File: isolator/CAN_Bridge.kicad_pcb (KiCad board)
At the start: 2 copper layers, 45 parts, among them J1 BOOT1, J2 BOOT0, J3 Power in, J4 JTAG5, J5 USART1, J7 HIGHVOLTAGE CAN, J8 LOWVOLTAGE CAN, SW2 SW_Push, U1 STM32F105RBTx, U2 ISO1050DUB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

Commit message: update isolator PCB
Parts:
- moved H1 9.60 mm to (135.4, 61.4)
- moved C1 1.10 mm to (144.7, 102.2)
- moved H1 0.71 mm to (135.4, 110.0)
- moved U2 0.70 mm to (169.5, 101.7)
- moved R6 0.20 mm to (160.2, 65.6)
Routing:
- net GND: track 29.8 -> 30.9 mm, vias 24 -> 23
- net HV_CANH: track 13.2 -> 14.2 mm
- net HV_CANL: track 13.0 -> 14.0 mm
- net +3.3V: track 127.8 -> 128.5 mm
- net HV_TXD: track 15.3 -> 14.6 mm
- net HV_RXD: track 14.4 -> 13.7 mm
- net +5P: track 19.5 -> 20.2 mm
- net GND2: track 3.71 -> 4.41 mm
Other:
- board outline added: 64 x 57.6 mm
- board text added: "12.7mm"

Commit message: Tweaks to schematic
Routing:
- net GND: track 30.9 -> 35.4 mm
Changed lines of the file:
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@@
   (segment (start 157.6625 84.8375) (end 159.3 84.8375) (width 1) (layer "F.Cu") (net 1))
   (segment (start 139.9 85.1625) (end 139.5 85.5625) (width 0.5) (layer "F.Cu") (net 2))
+  (segment (start 177.275 79.115) (end 177.275 77.425) (width 1) (layer "F.Cu") (net 2))
   (segment (start 144.13 82.05) (end 144.13 83.43) (width 0.5) (layer "F.Cu") (net 2))
   (segment (start 144.13 83.43) (end 144.8 84.1) (width 0.5) (layer "F.Cu") (net 2))
+  (segment (start 162.61 105.51) (end 162.5 105.4) (width 1) (layer "F.Cu") (net 2))
   (segment (start 139.9 83.8) (end 139.9 85.1625) (width 0.5) (layer "F.Cu") (net 2))
   (segment (start 171.75 66.425) (end 171.675 66.425) (width 0.5) (layer "F.Cu") (net 2))
@@
   (segment (start 144.15 87.08) (end 144.15 85.5875) (width 0.3) (layer "F.Cu") (net 2))
   (segment (start 171.75 66.425) (end 171.75 66.45) (width 0.5) (layer "F.Cu") (net 2))
+  (segment (start 177.275 77.425) (end 177.5 77.2) (width 1) (layer "F.Cu") (net 2))
+  (segment (start 164.975 105.51) (end 162.61 105.51) (width 1) (layer "F.Cu") (net 2))
   (via (at 144.8 84.1) (size 0.8) (drill 0.4) (layers "F.Cu" "B.Cu") (free) (net 2))
   (via (at 132.1 97.8) (size 0.8) (drill 0.4) (layers "F.Cu" "B.Cu") (free) (net 2))
@@
       (pts
         (xy 175.8 96.9)
-        (xy 172.6 96.9)
-        (xy 172.6 106.6)
+        (xy 175.8 96.9)
+        (xy 175.8 106.6)
         (xy 175.8 106.6)
         (xy 175.8 114.5)
@@
     (polygon
       (pts
-        (xy 166.4 106.5)
+        (xy 162.8 106.5)
         (xy 162.8 106.5)
         (xy 162.8 114.5)
@@
         (xy 130.9 56.9)
         (xy 194.9 56.9)
-        (xy 194.812446 77.4)
-        (xy 194.3 77.4)
-        (xy 194.3 80.2)
-        (xy 175.8 80.2)
+        (xy 194.812446 77.5)
+        (xy 194.3 77.5)
+        (xy 194.3 77.5)
+        (xy 175.8 77.5)
         (xy 175.8 77.5)
         (xy 170 77.5)
         (xy 162.8 85.9)
         (xy 162.8 96.8)
-        (xy 166.4 96.8)
+        (xy 162.8 96.8)
       )
     )

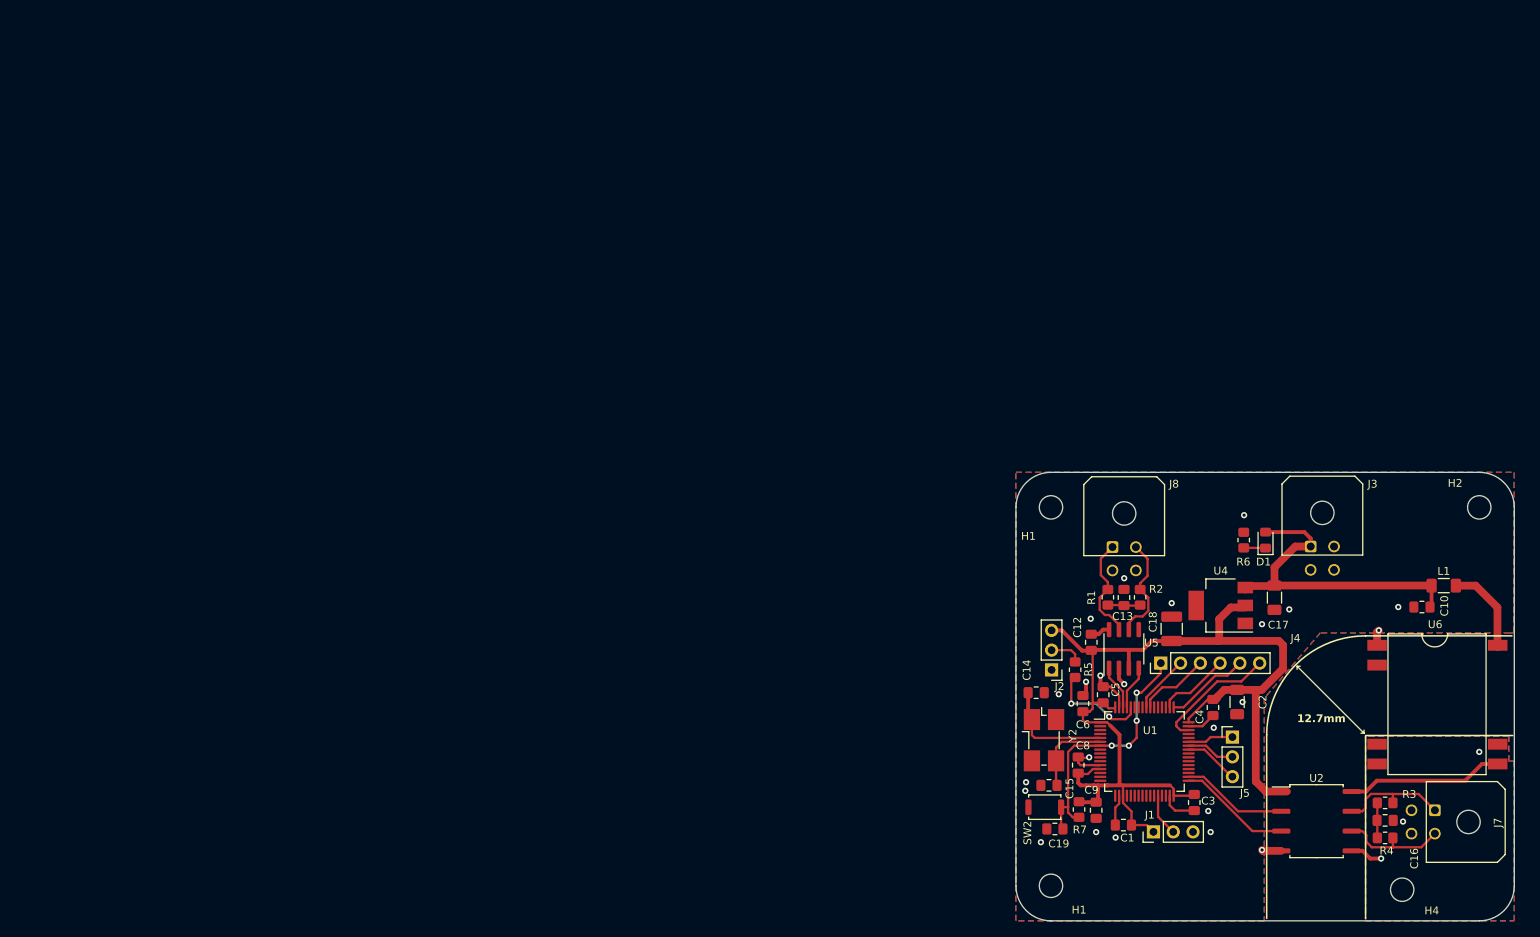
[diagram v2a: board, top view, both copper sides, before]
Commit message: Isolator tweaks
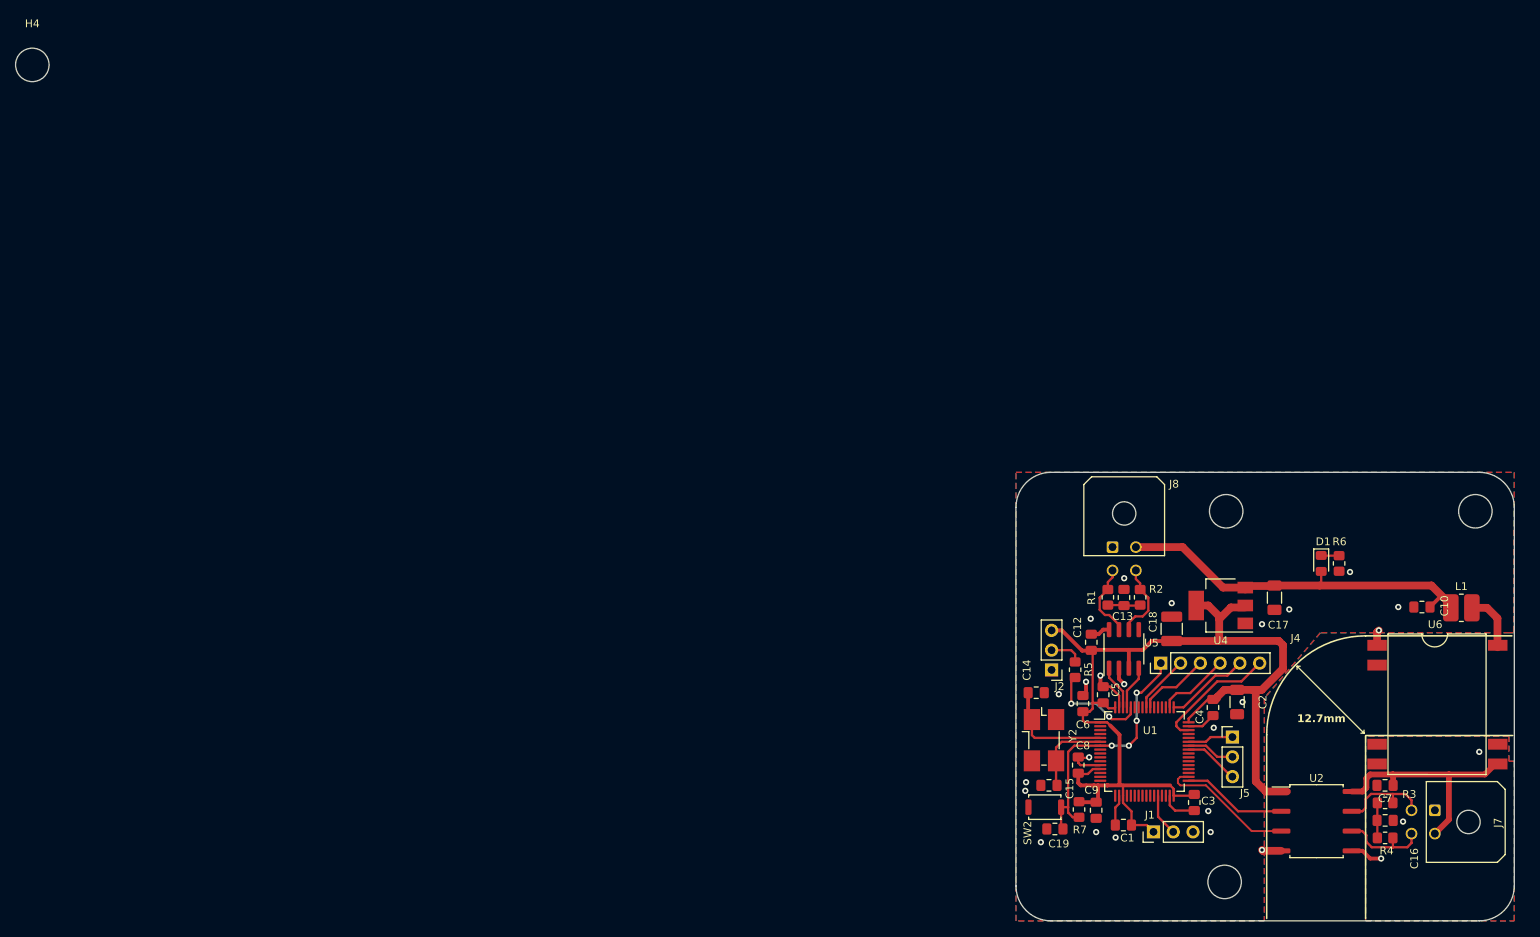
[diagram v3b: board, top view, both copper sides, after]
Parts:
- removed the H1 at (135.4, 110.0)
- removed the H1 at (135.4, 61.4)
- removed J3: Power in, Connector_Molex:Molex_Micro-Fit_3.0_43045-0400_2x02_P3.00mm_Horizontal
- added C7: 10u, Capacitor_SMD:C_0805_2012Metric_Pad1.18x1.45mm_HandSolder, F.Cu at (178.3, 97.1)
- added H1: MountingHole, MountingHole:MountingHole_4.3mm_M4, F.Cu at (157.7, 109.5)
- added H3: MountingHole, MountingHole:MountingHole_4.3mm_M4, F.Cu at (189.9, 61.9)
- H2, H4: footprint MountingHole:MountingHole_3mm -> MountingHole:MountingHole_4.3mm_M4
- L1: footprint Capacitor_SMD:C_1206_3216Metric_Pad1.33x1.80mm_HandSolder -> SUFST:RLS-397
- U4: footprint Package_TO_SOT_SMD:SOT-223 -> Package_TO_SOT_SMD:SOT-223-3_TabPin2
- U6: footprint Library:SMDIP-14_15.5mm -> SUFST:SMDIP-14_15.5mm
- Y2: value Crystal_GND24_Small -> 406C35E25M00000
- moved H4 205.4 mm to (4.58, 4.58)
- moved H2 32.5 mm to (157.9, 61.9)
- moved R6 12.6 mm to (172.4, 68.6), turned to 90 degrees
- moved D1 7.75 mm to (170.1, 68.6), turned to -90 degrees
- moved L1 3.64 mm to (188.1, 74.3)
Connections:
- net LV_RXD renamed MCU_CAN1_TX
- net LV_TXD renamed MCU_CAN1_RX
- J7 pad 1: HV_CANH -> GND2
- J7 pad 2: HV_CANL -> +5P
- J7 pad 3: (no net) -> HV_CANH
- J7 pad 4: (no net) -> HV_CANL
- J8 pad 1: LV_CANH -> GND
- J8 pad 2: LV_CANL -> +12V
- J8 pad 3: (no net) -> LV_CANH
- J8 pad 4: (no net) -> LV_CANL
- U1 pad 33: HV_TXD -> MCU_CAN2_RX
- U1 pad 34: HV_RXD -> MCU_CAN2_TX
- U2 pad 2: HV_RXD -> MCU_CAN2_RX
- U2 pad 3: HV_TXD -> MCU_CAN2_TX
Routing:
- net MCU_CAN2_TX: track 0.00 -> 17.8 mm
- net HV_TXD: track 14.6 -> 0.00 mm
- net HV_RXD: track 13.7 -> 0.00 mm
- net MCU_CAN2_RX: track 0.00 -> 13.5 mm
- net +5P: track 20.2 -> 30.7 mm
- net +12V: track 42.2 -> 50.2 mm
- net Net-(U6-+VIN): track 11.2 -> 7.17 mm
- net +3.3V: track 128.5 -> 132.4 mm
- net LV_CANL: track 14.2 -> 10.4 mm
- net LV_CANH: track 13.4 -> 9.63 mm
- net HV_CANL: track 14.0 -> 11.7 mm
- net HV_CANH: track 14.2 -> 12.0 mm

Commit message: Isolator done, pending review
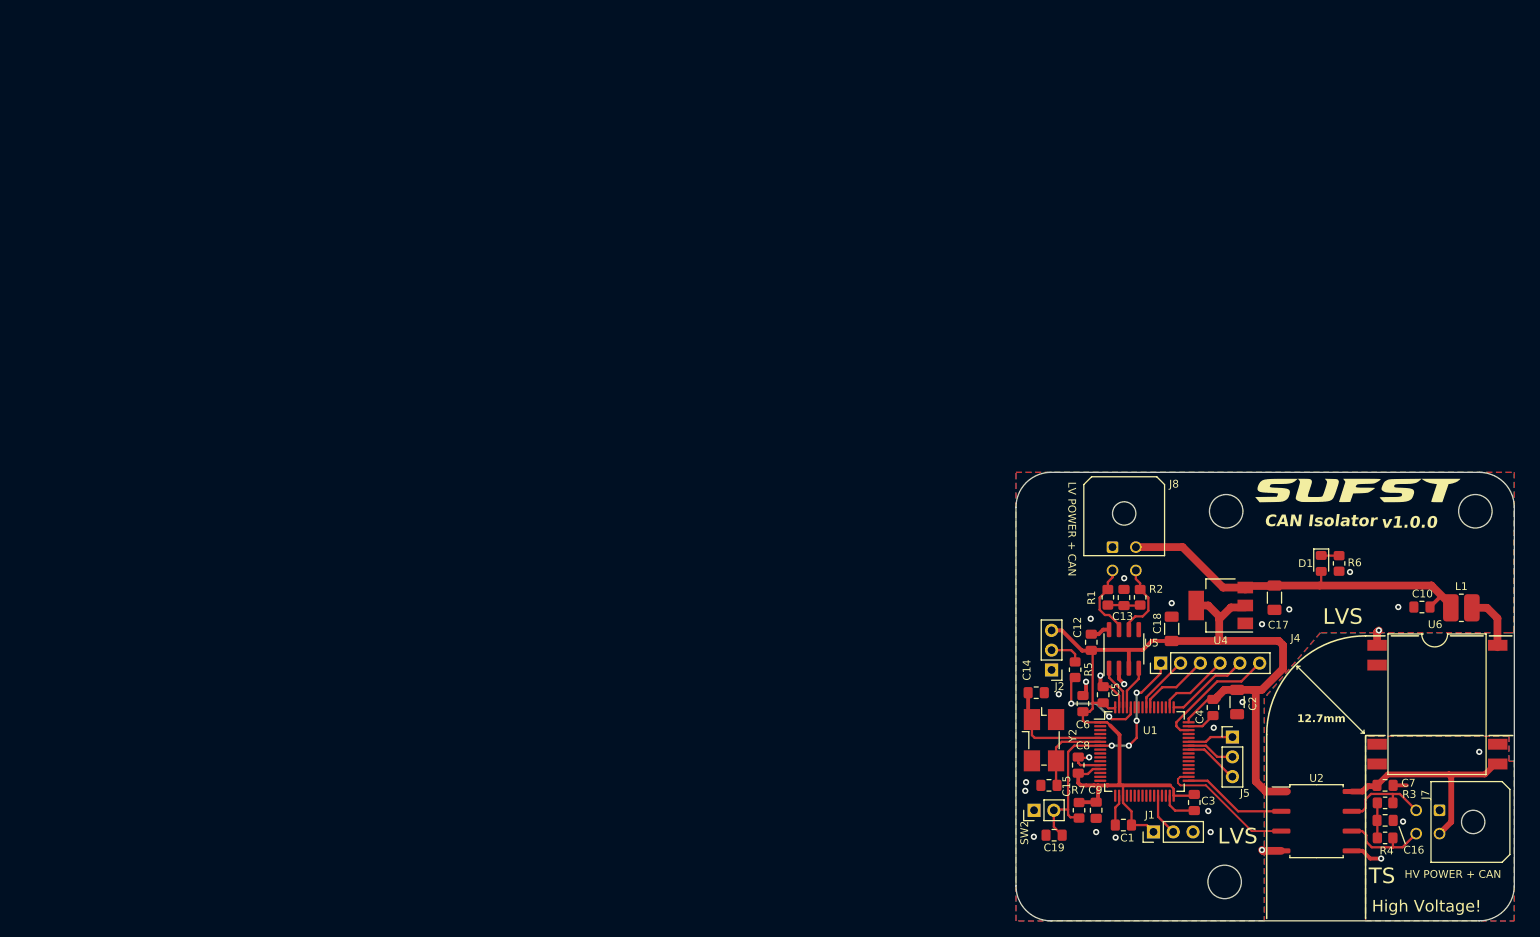
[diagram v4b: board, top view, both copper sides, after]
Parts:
- removed H4: MountingHole, MountingHole:MountingHole_4.3mm_M4
- added G***: LOGO, SUFST:sufst-text, F.Cu at (174.8, 59.2)
- C18: footprint Capacitor_SMD:C_1210_3225Metric_Pad1.33x2.70mm_HandSolder -> Capacitor_SMD:C_1206_3216Metric_Pad1.33x1.80mm_HandSolder
- SW2: footprint Button_Switch_SMD:SW_Push_SPST_NO_Alps_SKRK -> Connector_PinHeader_2.54mm:PinHeader_1x02_P2.54mm_Vertical
- moved SW2 1.43 mm to (133.2, 100.3), turned to 90 degrees
- moved C19 0.81 mm to (135.8, 103.5), turned to 180 degrees
- moved J7 0.60 mm to (185.3, 100.3)
- moved R7 0.10 mm to (139.0, 100.3), turned to 90 degrees
- turned C7 to 0 degrees
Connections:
- C19 pad 1: GND -> NReset
- C19 pad 2: NReset -> GND
- R7 pad 1: +3.3V -> NReset
- R7 pad 2: NReset -> +3.3V
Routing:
- net +5P: track 30.7 -> 28.6 mm
- net NReset: track 34.0 -> 35.9 mm
- net GND2: track 4.41 -> 6.17 mm
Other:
- board text added: "+12V"
- board text added: "CAN Isolator"
- board text added: "GND"
- board text added: "HV POWER + CAN"
- board text added: "HV_5V"
- board text added: "HV_CANH"
- board text added: "HV_CANL"
- board text added: "HV_GND"
- board text added: "High Voltage!"
- board text added: "LV POWER + CAN"
- board text added: "LVS"
- board text added: "LV_CANH"
- board text added: "LV_CANL"
- board text added: "TS"
- board text added: "v1.0.0"

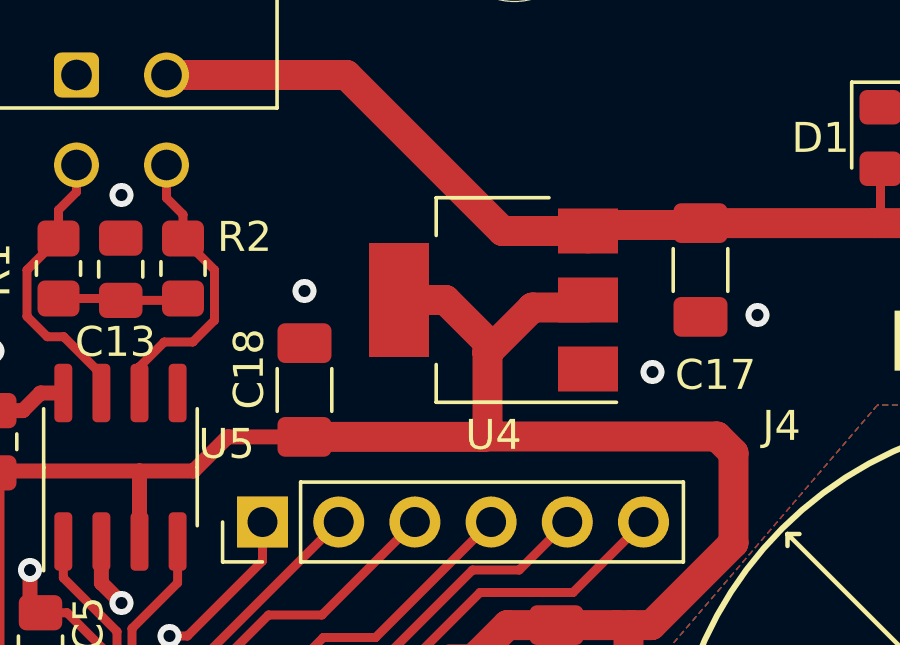
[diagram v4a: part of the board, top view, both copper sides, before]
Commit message: Larger pad on linear reg
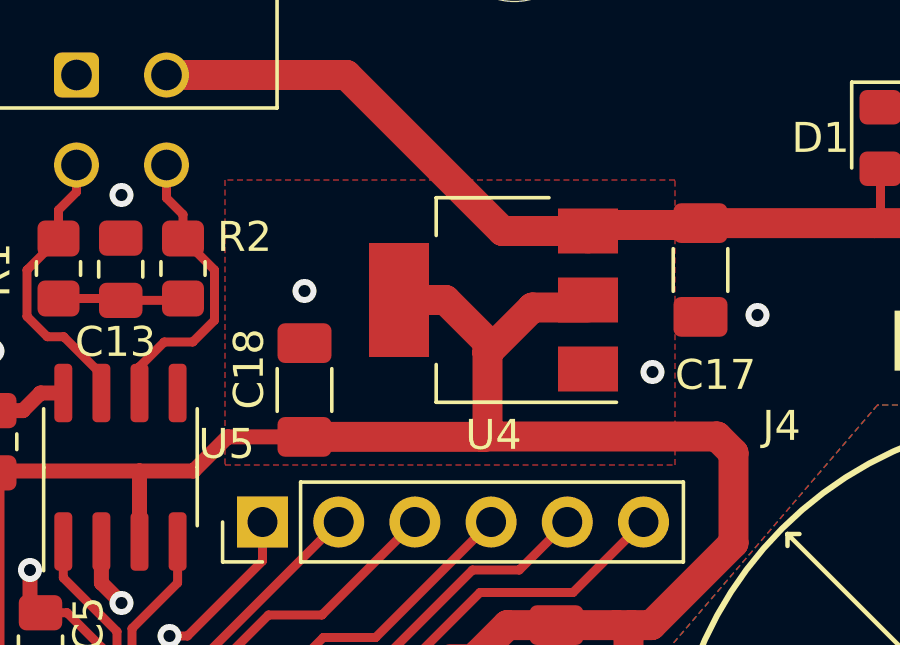
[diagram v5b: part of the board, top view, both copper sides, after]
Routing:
- added copper zone on F.Cu, net +3.3V
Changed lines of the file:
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@@
   (segment (start 146.4 85.2) (end 146.4 88.8) (width 0.3) (layer "B.Cu") (net 72))
   (segment (start 143.2 92) (end 145.4 92) (width 0.3) (layer "B.Cu") (net 72))
+  (zone (net 1) (net_name "+3.3V") (layer "F.Cu") (hatch edge 0.5)
+    (priority 2)
+    (connect_pads (clearance 0.5))
+    (min_thickness 0.25) (filled_areas_thickness no)
+    (fill yes (thermal_gap 0.5) (thermal_bridge_width 0.5))
+    (polygon
+      (pts
+        (xy 148.25 70)
+        (xy 148.25 79.5)
+        (xy 163.25 79.5)
+        (xy 163.25 70)
+      )
+    )
+  )
   (zone (net 9) (net_name "GND2") (layers "F&B.Cu") (hatch edge 0.5)
     (priority 1)

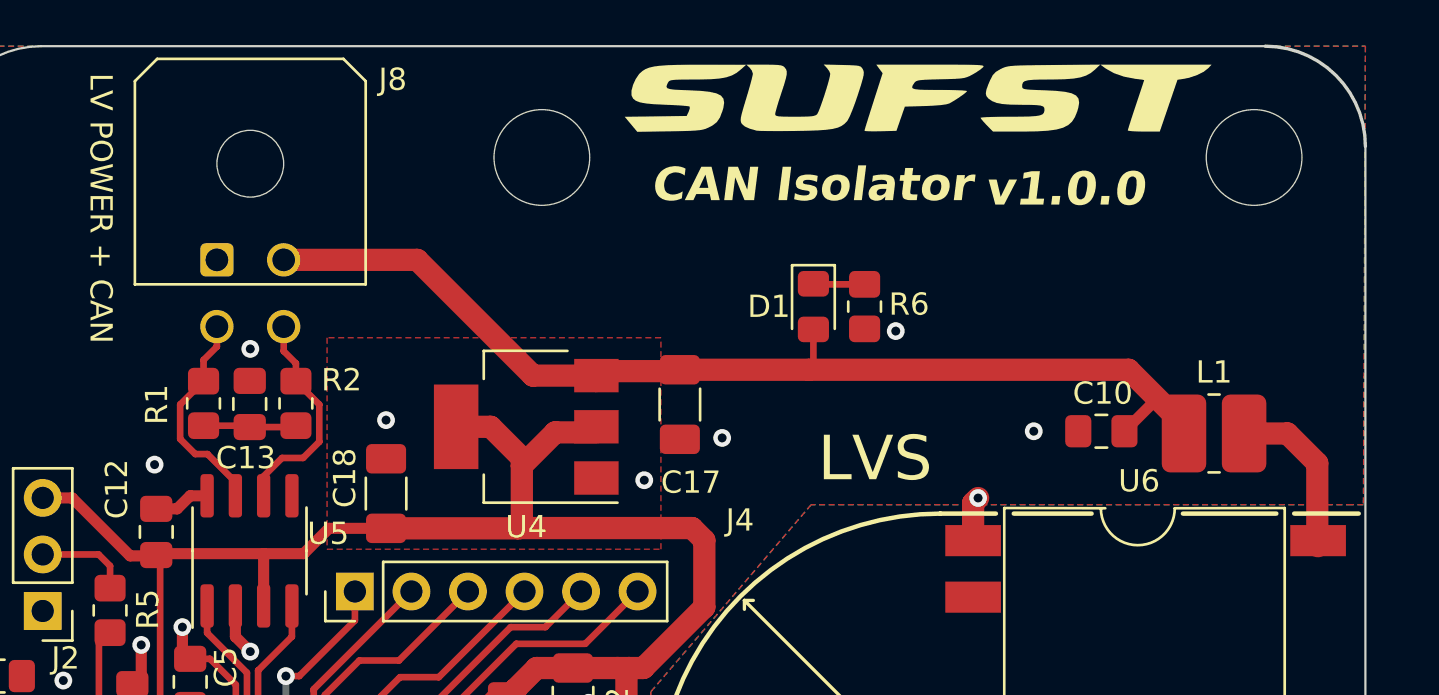
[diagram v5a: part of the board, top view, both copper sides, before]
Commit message: step files for STAG12
moved connector on PCB, needs revamp still
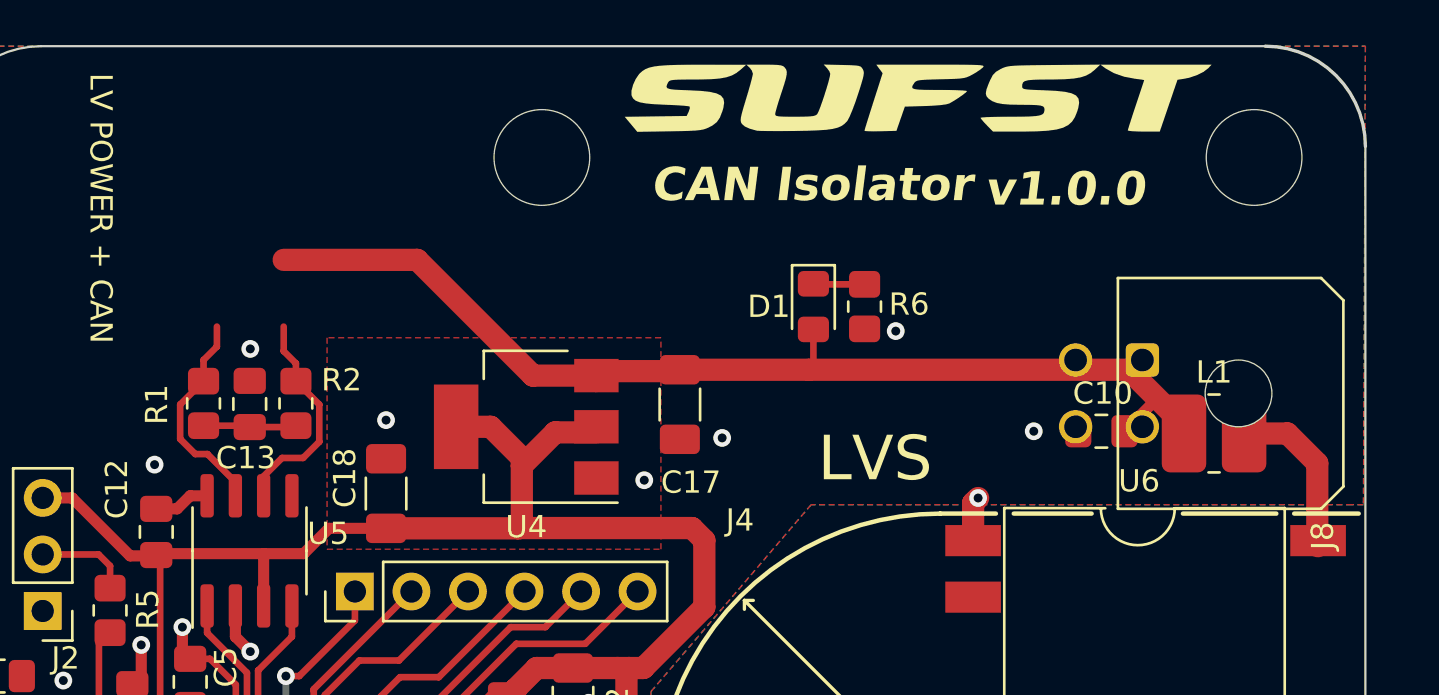
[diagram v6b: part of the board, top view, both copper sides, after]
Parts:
- moved J8 41.8 mm to (184.9, 71.0), turned to -90 degrees
